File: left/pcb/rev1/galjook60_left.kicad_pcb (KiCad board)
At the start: 2 copper layers, 88 parts, among them SW1 SW_Push, U1 ATmega32U4-AU, U2 TRRS, Y1 16MHz

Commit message: Finalized PCB for the left side
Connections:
- U1 pad 1: Net-(U1-Pad1) -> col0
- U1 pad 11: Net-(U1-Pad11) -> row1
- U1 pad 12: Net-(U1-Pad12) -> row0
- U1 pad 18: Net-(U1-Pad18) -> col1
- U1 pad 19: Net-(U1-Pad19) -> col5
- U1 pad 22: Net-(U1-Pad22) -> Split1
- U1 pad 25: Net-(U1-Pad25) -> col2
- U1 pad 26: Net-(U1-Pad26) -> col3
- U1 pad 27: Net-(U1-Pad27) -> col4
- U1 pad 30: Net-(U1-Pad30) -> col7
- U1 pad 38: Net-(U1-Pad38) -> col6
- U1 pad 39: Net-(U1-Pad39) -> row4
- U1 pad 40: Net-(U1-Pad40) -> row3
- U1 pad 41: Net-(U1-Pad41) -> row2
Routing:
- net col7: track 0.00 -> 133.0 mm, vias 0 -> 4
- net Split1: track 0.00 -> 120.4 mm, vias 0 -> 2
- net col6: track 58.8 -> 167.6 mm, vias 0 -> 3
- net col5: track 93.0 -> 196.5 mm, vias 0 -> 2
- net col4: track 88.0 -> 149.3 mm, vias 0 -> 1
- net row4: track 136.1 -> 189.3 mm, vias 0 -> 4
- net col3: track 90.0 -> 127.0 mm, vias 0 -> 1
- net row3: track 129.5 -> 155.6 mm, vias 0 -> 2
- net col2: track 91.9 -> 109.9 mm, vias 0 -> 1
- net row0: track 143.1 -> 160.3 mm, vias 2 -> 4
- net col0: track 81.3 -> 96.2 mm, vias 1 -> 3
- net row1: track 126.4 -> 137.2 mm, vias 0 -> 2
- net col1: track 92.1 -> 101.4 mm
- net row2: track 125.0 -> 132.7 mm, vias 0 -> 2
- added copper zone on B.Cu, net (none)
- added copper zone on B.Cu, net GND
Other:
- board outline added: 157.2 x 95.2 mm
- board text added: "Galjook60 Rev 1.0"

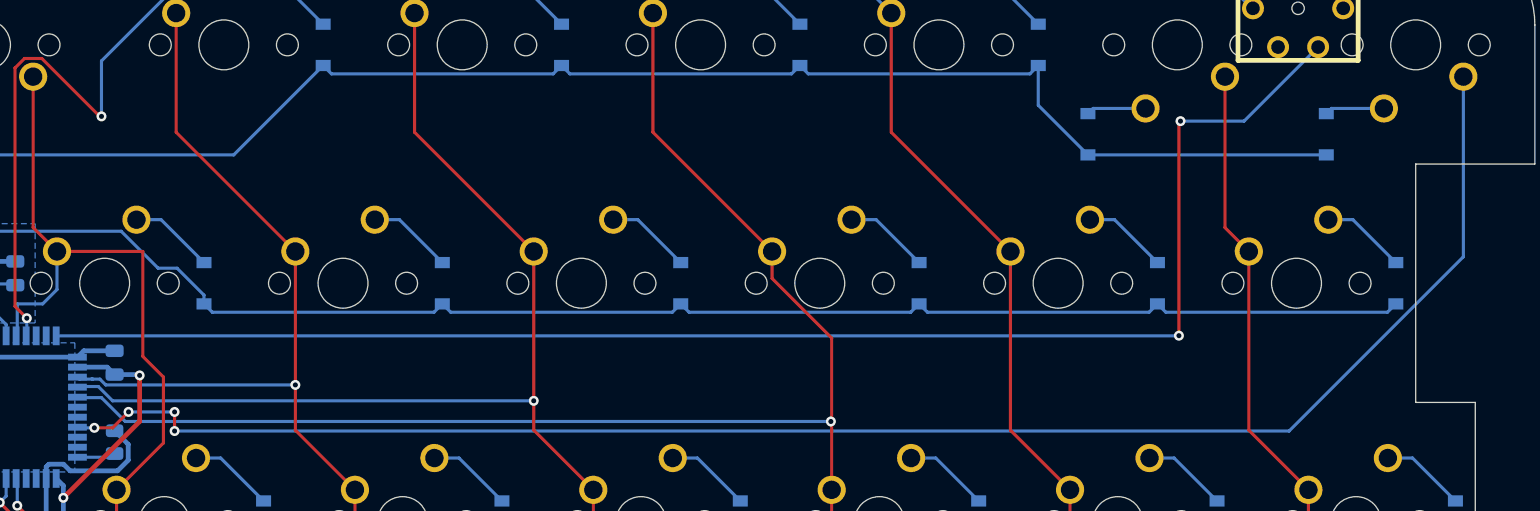
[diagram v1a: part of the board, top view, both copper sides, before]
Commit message: Added schematic for the PCB for the right side
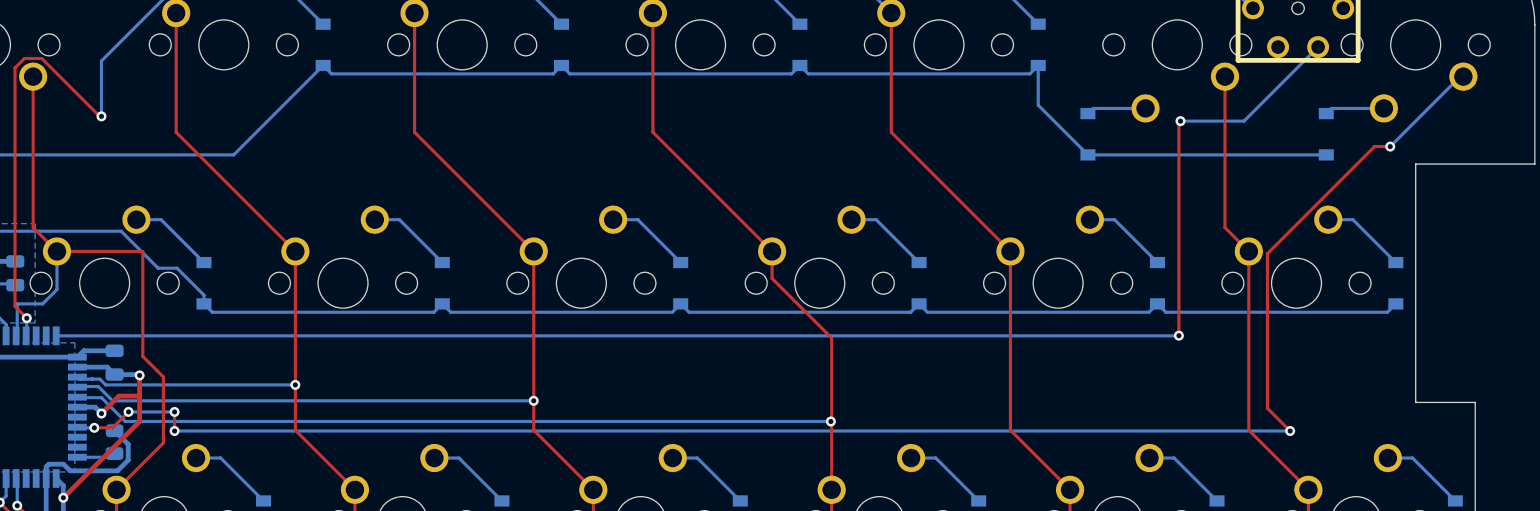
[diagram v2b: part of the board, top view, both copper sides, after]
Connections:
- U1 pad 28: Net-(U1-Pad28) -> +5V
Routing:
- net +5V: track 231.3 -> 237.0 mm, vias 6 -> 7
- net col7: track 133.0 -> 135.4 mm, vias 4 -> 6

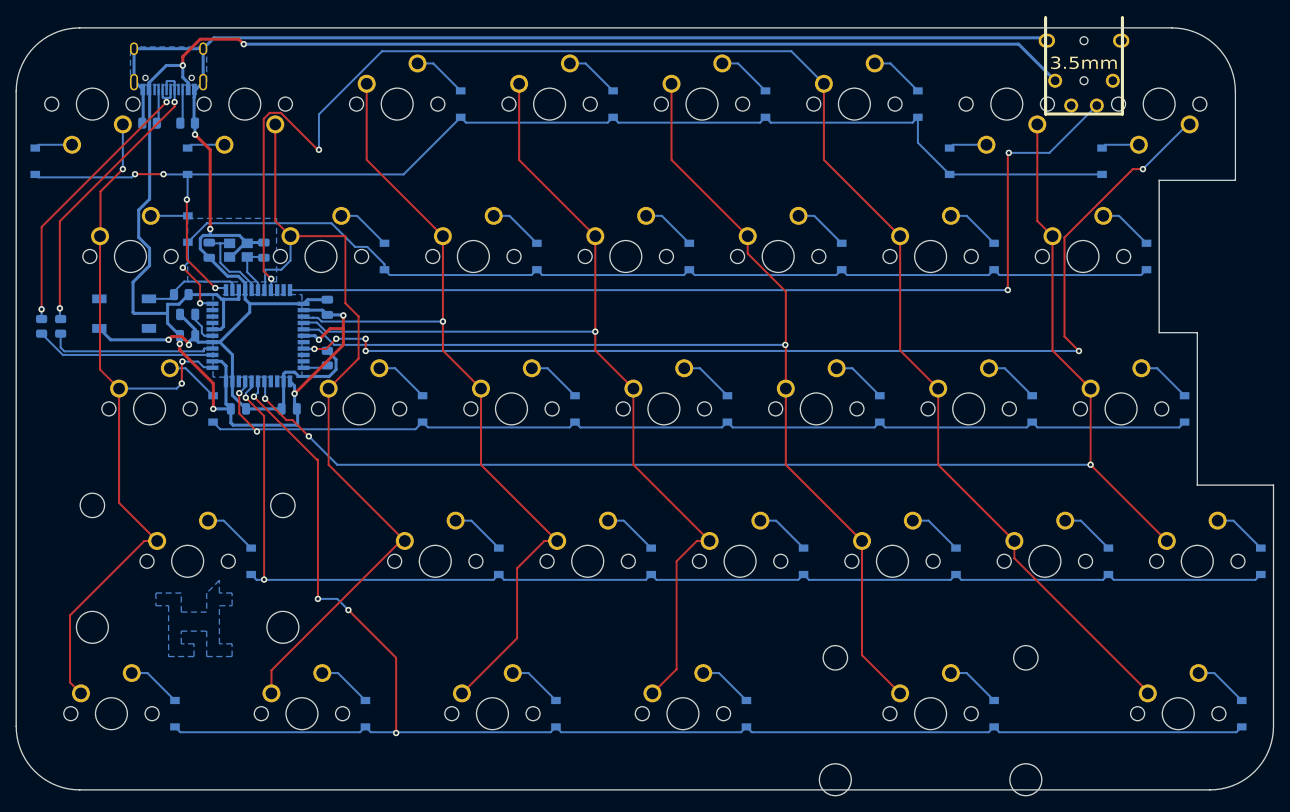
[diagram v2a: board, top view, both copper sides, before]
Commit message: added full PCB for the right side
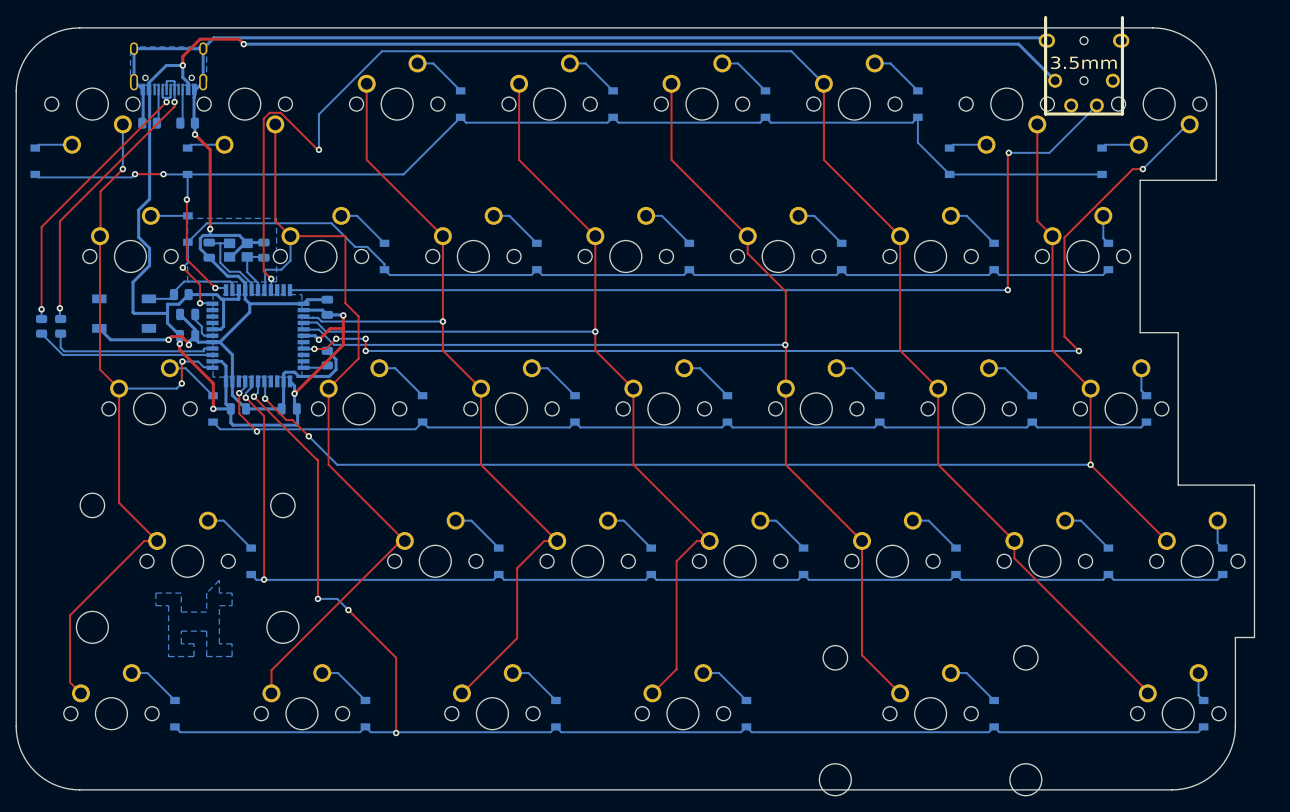
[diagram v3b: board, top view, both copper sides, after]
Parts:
- moved D33 4.76 mm to (220.7, 127.0)
- moved D30 4.76 mm to (227.8, 165.1)
- moved D32 4.76 mm to (215.9, 108.0)
- moved D34 4.76 mm to (230.2, 146.1)
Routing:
- net row3: track 155.6 -> 150.8 mm
- net row2: track 132.7 -> 128.0 mm
- net row1: track 137.2 -> 132.4 mm
- net row4: track 189.3 -> 184.5 mm
- net Net-(D33-Pad2): track 6.82 -> 3.69 mm
- net Net-(D34-Pad2): track 6.82 -> 3.69 mm
- net Net-(D30-Pad2): track 6.82 -> 3.69 mm
- net Net-(D32-Pad2): track 6.82 -> 3.69 mm
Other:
- board size 157.2 x 95.2 mm -> 154.8 x 95.2 mm

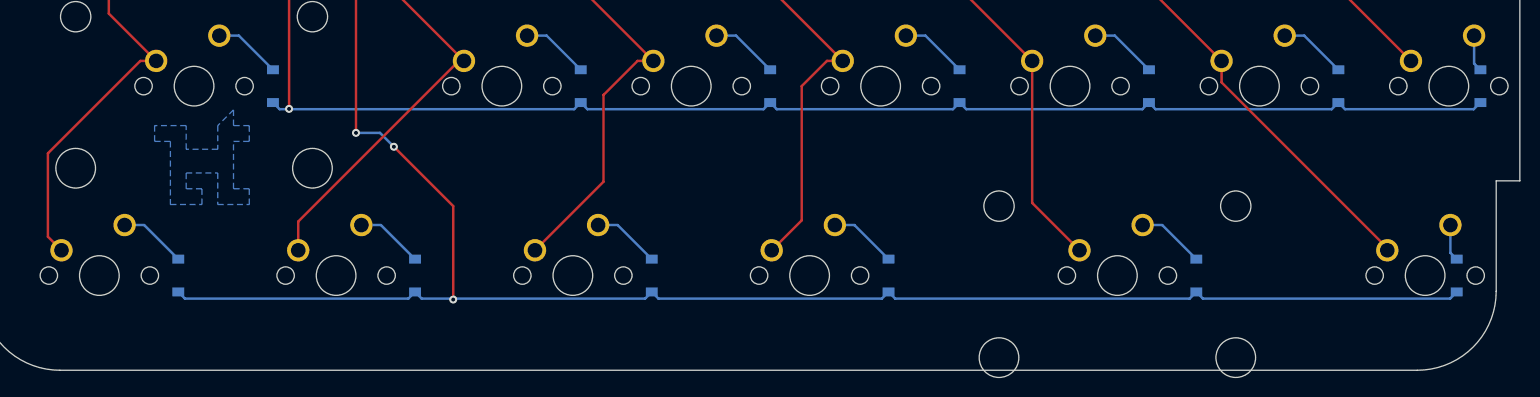
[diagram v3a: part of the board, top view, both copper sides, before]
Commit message: updated left side PCB to reflect other split keyboards
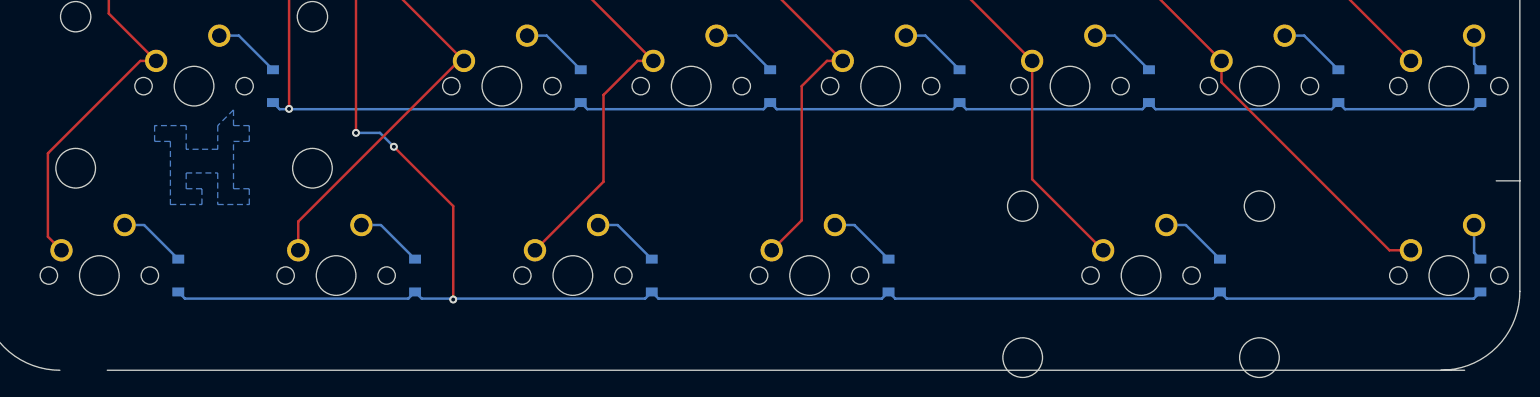
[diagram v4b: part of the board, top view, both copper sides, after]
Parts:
- MX25: footprint MX_Only:MXOnly-2U-NoLED -> MX_Only:MXOnly-2.25U-NoLED
- MX30: footprint MX_Only:MXOnly-1.25U-NoLED -> MX_Only:MXOnly-1U-NoLED
- moved D25 2.38 mm to (204.0, 165.1)
- moved D30 2.38 mm to (230.2, 165.1)
- moved MX25 2.38 mm to (196.1, 165.1)
- moved MX30 2.38 mm to (227.0, 165.1)
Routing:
- net col5: track 196.5 -> 199.0 mm
- net row4: track 184.5 -> 186.9 mm
- net col4: track 149.3 -> 150.3 mm
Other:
- outline, holes or cut-outs redrawn
